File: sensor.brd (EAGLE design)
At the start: 76 x 50 mm, 32 parts, among them IC1 TP4056, U1 NX1117C33Z, U3 BMP180, U4 TSL2561, Y1 12mhz

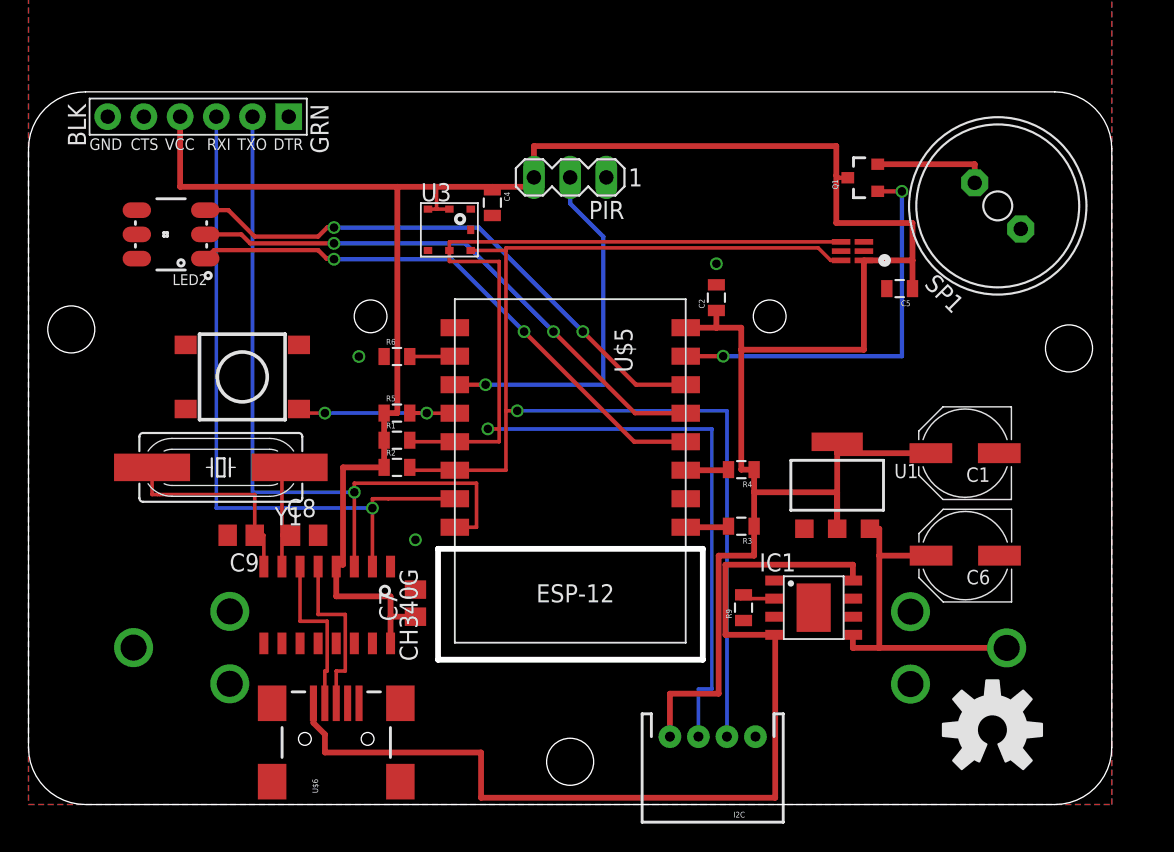
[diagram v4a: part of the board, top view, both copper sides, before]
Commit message: Redone this time without the esp8266's housing clipping through the PIR variable resistors
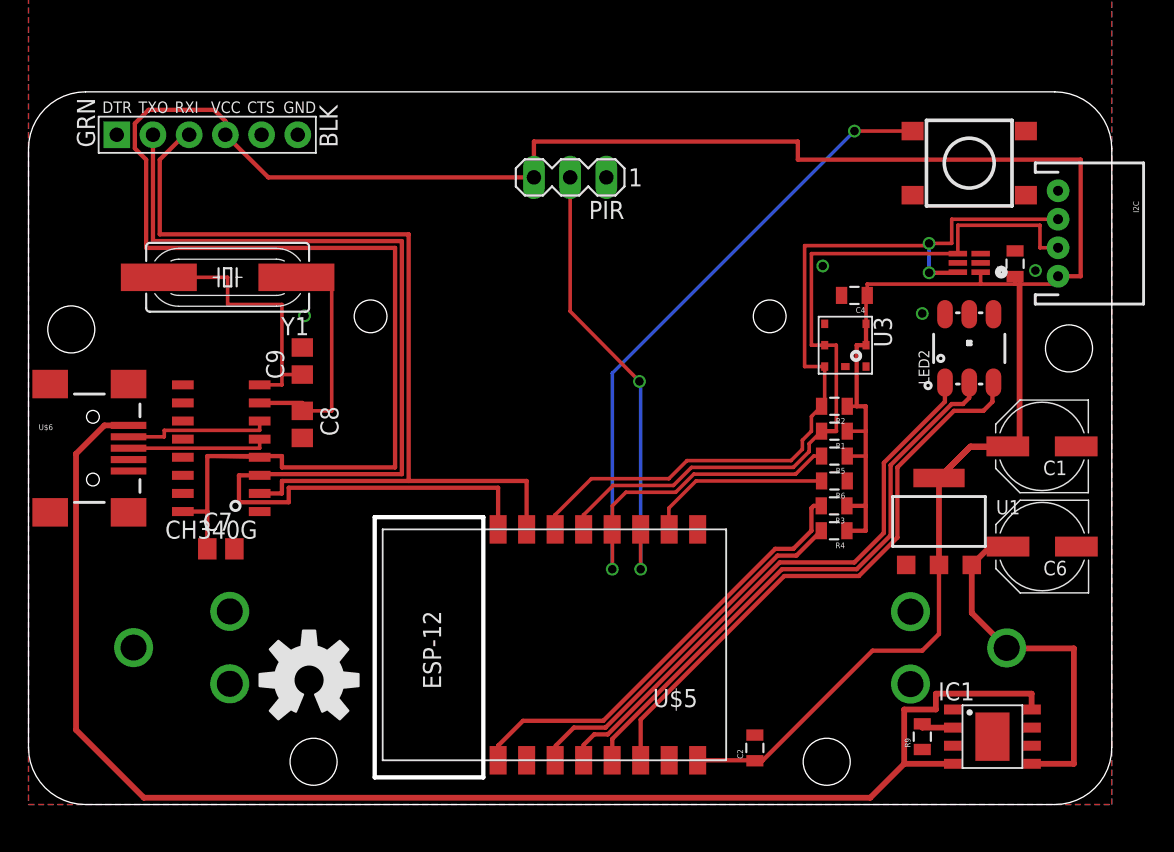
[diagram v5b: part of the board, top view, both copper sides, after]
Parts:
- removed Q1: (no value), SparkFun-DiscreteSemi:SOT23-3
- removed SP1: SPEAKER/AL11P, adafruit:AL11P
- moved LED2 56.6 mm to (66.0, 32.0), turned to 90 degrees
- moved S1 53.2 mm to (66.0, 45.0), turned to 180 degrees
- moved LOGO1 48.1 mm to (19.7, 8.73)
- moved I2C 42.8 mm to (72.2, 40.1), turned to 270 degrees
- moved U$5 32.5 mm to (48.9, 3.10), turned to 90 degrees
- moved R6 31.9 mm to (56.5, 22.7), turned to 180 degrees
- moved C2 31.7 mm to (51.0, 3.97)
- moved R2 31.0 mm to (56.5, 27.9), turned to 180 degrees
- moved R5 30.8 mm to (56.5, 24.4), turned to 180 degrees
- moved R1 30.7 mm to (56.5, 26.2), turned to 180 degrees
- moved U3 28.9 mm to (57.3, 32.2), turned to 270 degrees
- moved U$6 26.6 mm to (4.52, 25.0), turned to 0 degrees
- moved C4 26.2 mm to (57.9, 35.7), turned to 180 degrees
- moved IC1 15.5 mm to (67.6, 4.76)
- moved R9 15.5 mm to (62.7, 4.76)
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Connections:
- removed net N$6: Q1.2, SP1.+
- net 3.3V: no longer Q1.3
- net GND: no longer SP1.-
- net GPIO13: no longer Q1.1
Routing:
- net 3.3V: track 195.9 -> 245.5 mm
- net GPIO0: track 13.6 -> 62.4 mm
- net 5V: track 68.4 -> 103.4 mm
- net SCL: track 90.4 -> 56.6 mm, vias 1 -> 0
- net RESET: track 3.07 -> 31.6 mm
- net GPIO13: track 28.5 -> 0.00 mm, vias 2 -> 0
- net SDA: track 87.3 -> 60.5 mm, vias 1 -> 2
- net TX: track 52.5 -> 76.8 mm, vias 1 -> 0
- net CHPD: track 3.04 -> 25.9 mm
- net RX: track 49.0 -> 65.8 mm, vias 1 -> 0
- net GPIO15: track 3.18 -> 13.0 mm
- net OSCI: track 8.14 -> 17.5 mm
- net N$6: track 8.11 -> 0.00 mm
- net GPIO2: track 25.9 -> 32.4 mm, vias 1 -> 2
- net OSCO: track 14.8 -> 19.2 mm
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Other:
- outline, holes or cut-outs redrawn

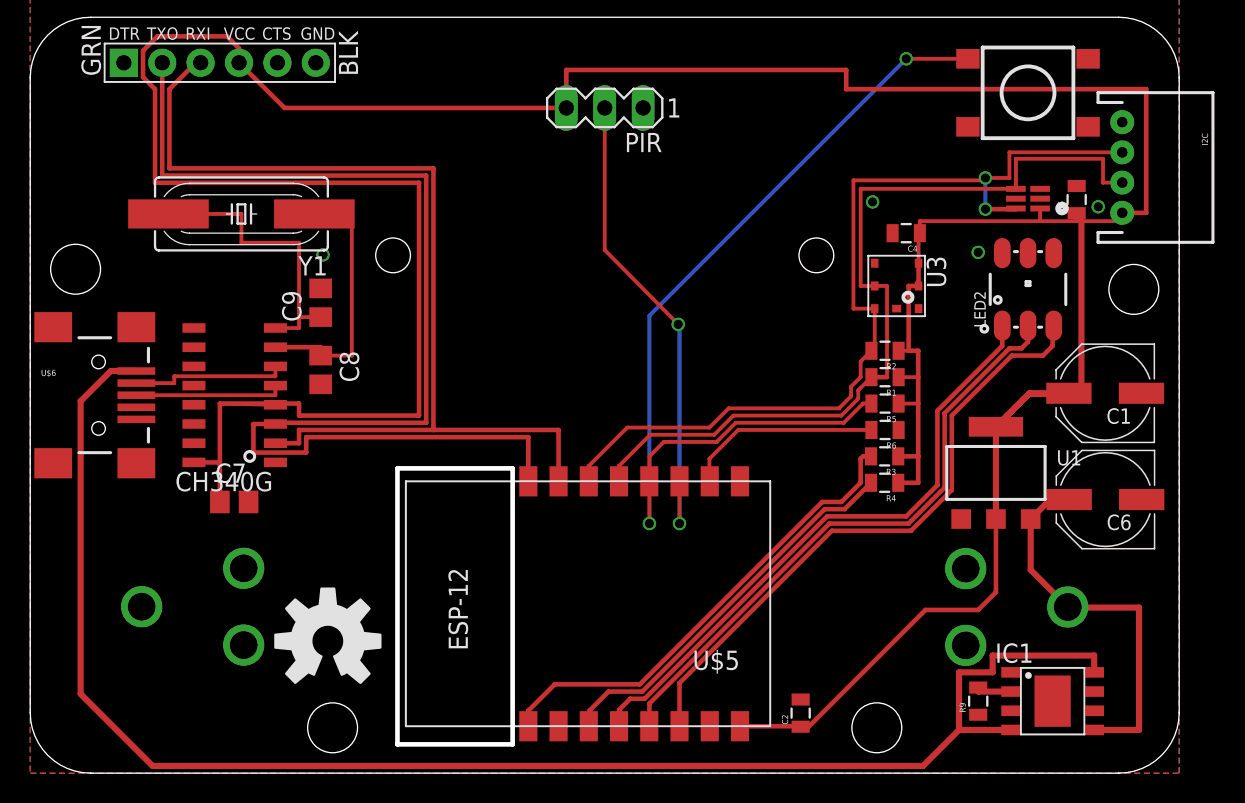
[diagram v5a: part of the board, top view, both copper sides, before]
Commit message: Moving to using MCP7381 and TPS63001.. Damn tiny ass packages.
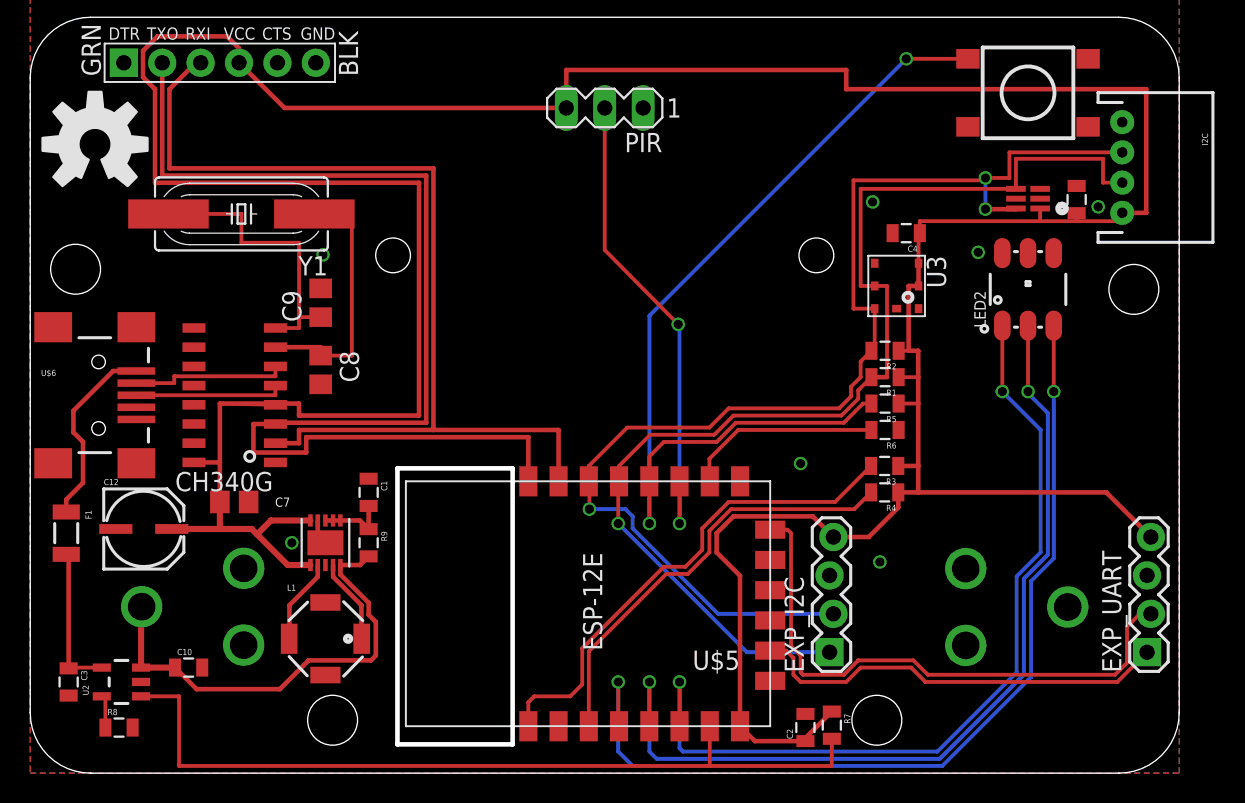
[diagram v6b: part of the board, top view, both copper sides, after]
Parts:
- removed C6: (no value), SparkFun-Capacitors:PANASONIC_D
- removed IC1: TP4056, TP4056:SOP-8
- removed U1: NX1117C33Z, nxp_60:SOT223
- added C10, C3: 10uf, SparkFun-Capacitors:0805
- added C12: 47uf, SparkFun-Capacitors:PANASONIC_C
- added EXP_I2C, EXP_UART: (no value), SparkFun-Connectors:1X04_LOCK
- added F1: 500mA, SparkFun:PTC-1206
- added L1: 2.2uH, SparkFun-Passives:SRU5028
- added R7, R8: 2k, SparkFun-Resistors:0805
- added U2: MCP73831, SparkFun:SOT23-5
- added U6: TPS63001DRCR, Texas Instruments_By_element14_Batch_1:SON50P300X300X100-11N
- C1: value (none) -> 0.1uf; device SparkFun-Capacitors:PANASONIC_D -> SparkFun-Capacitors:0805
- R9: value 122 -> 100
- U$5: value ESP8266_ESP-12 -> (none); device ESP8266-ESP12:ESP8266-ESP12 -> ESP8266-ESP12E:ESP8266-ESP12E
- moved C1 49.2 mm to (22.4, 18.6), turned to 270 degrees
- moved R9 41.7 mm to (22.4, 15.2), turned to 270 degrees
- moved LOGO1 36.3 mm to (4.29, 41.6)
- moved C2 1.00 mm to (51.3, 3.02)
- moved R3 0.63 mm to (56.5, 20.3)
- moved R4 0.63 mm to (56.5, 18.6)
- turned BAT1 to 180 degrees
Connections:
- removed net 5V: IC1.4, IC1.8, U$6.VBUS
- removed net GPIO0: R5.2, S1.A2, U$5.4
- removed net GPIO12: LED2.3, U$5.14
- removed net GPIO13: U$5.15
- removed net GPIO14: LED2.2, U$5.13
- removed net GPIO16: LED2.1, U$5.12
- removed net GPIO2: PIR.2, U$5.3
- removed net N$3: IC1.2, R9.2
- new net 5VIN: C3.1, F1.2, U2.4
- new net 5V_USB: F1.1, U$6.VBUS
- new net LED_B: LED2.3, U$5.4
- new net LED_G: LED2.1, U$5.6
- new net LED_R: LED2.2, U$5.5
- new net N$1: L1.2, U6.2
- new net N$11: R8.1, U2.5
- new net N$2: L1.1, U6.4
- new net SENSE: PIR.2, U$5.11
- new net SOFT_RX: EXP_UART.2, U$5.20
- new net SOFT_TX: EXP_UART.1, U$5.19
- new net STAT: R7.2, U$5.7, U2.1
- new net SWITCH: R5.2, S1.A2, U$5.12
- new net VINA: C1.2, R9.1, U6.6, U6.7, U6.8
- net 3.3V: now also C12.+, EXP_I2C.4, EXP_UART.4, R7.1, U$5.8, U6.1, U6.10; no longer C1.+, U$5.16, U1.2, U1.4
- net ADC: now also U$5.2; no longer U$5.10
- net CHPD: now also U$5.3; no longer U$5.11
- net GND: now also C1.1, C10.2, C12.-, C3.2, EXP_I2C.3, EXP_UART.3, R8.2, U$5.9, U2.2, U6.11, U6.3, U6.9; no longer C1.-, C6.-, IC1.1, IC1.3, R9.1, U$5.1, U1.1
- net GPIO15: now also U$5.10; no longer U$5.2
- net RESET: now also U$5.1; no longer U$5.9
- net RX: now also U$5.15; no longer U$5.7
- net SCL: now also EXP_I2C.1, U$5.13; no longer U$5.5
- net SDA: now also EXP_I2C.2, U$5.14; no longer U$5.6
- net TX: now also U$5.16; no longer U$5.8
- net V_BATT: now also C10.1, R9.2, U2.3, U6.5; no longer C6.+, IC1.5, U1.3
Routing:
- net 5V: track 103.4 -> 0.00 mm
- net SWITCH: track 0.00 -> 62.4 mm, vias 0 -> 2
- net GPIO0: track 62.4 -> 0.00 mm, vias 2 -> 0
- net LED_B: track 0.00 -> 61.6 mm, vias 0 -> 2
- net LED_R: track 0.00 -> 59.1 mm, vias 0 -> 2
- net LED_G: track 0.00 -> 56.5 mm, vias 0 -> 2
- net STAT: track 0.00 -> 54.7 mm
- net GPIO12: track 41.0 -> 0.00 mm
- net GPIO16: track 40.6 -> 0.00 mm
- net GPIO14: track 40.4 -> 0.00 mm
- net SOFT_RX: track 0.00 -> 38.0 mm
- net SENSE: track 0.00 -> 32.4 mm, vias 0 -> 2
- net GPIO2: track 32.4 -> 0.00 mm, vias 2 -> 0
- net SOFT_TX: track 0.00 -> 28.0 mm
- net SDA: track 60.5 -> 81.9 mm, vias 2 -> 3
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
